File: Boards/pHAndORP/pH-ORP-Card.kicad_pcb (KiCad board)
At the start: 4 copper layers, 80 x 72 mm, 120 parts, among them IC1 PIC32MM0064GPM028, Q1 NX7002AK, Q2 NX7002AK, Q3 NX7002AK, Q4 AO3407A, Q5 MMBT3904, Q6 MMBT3904, Q7 AO3407A, Q8 AO3407A, U1 AP2114H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

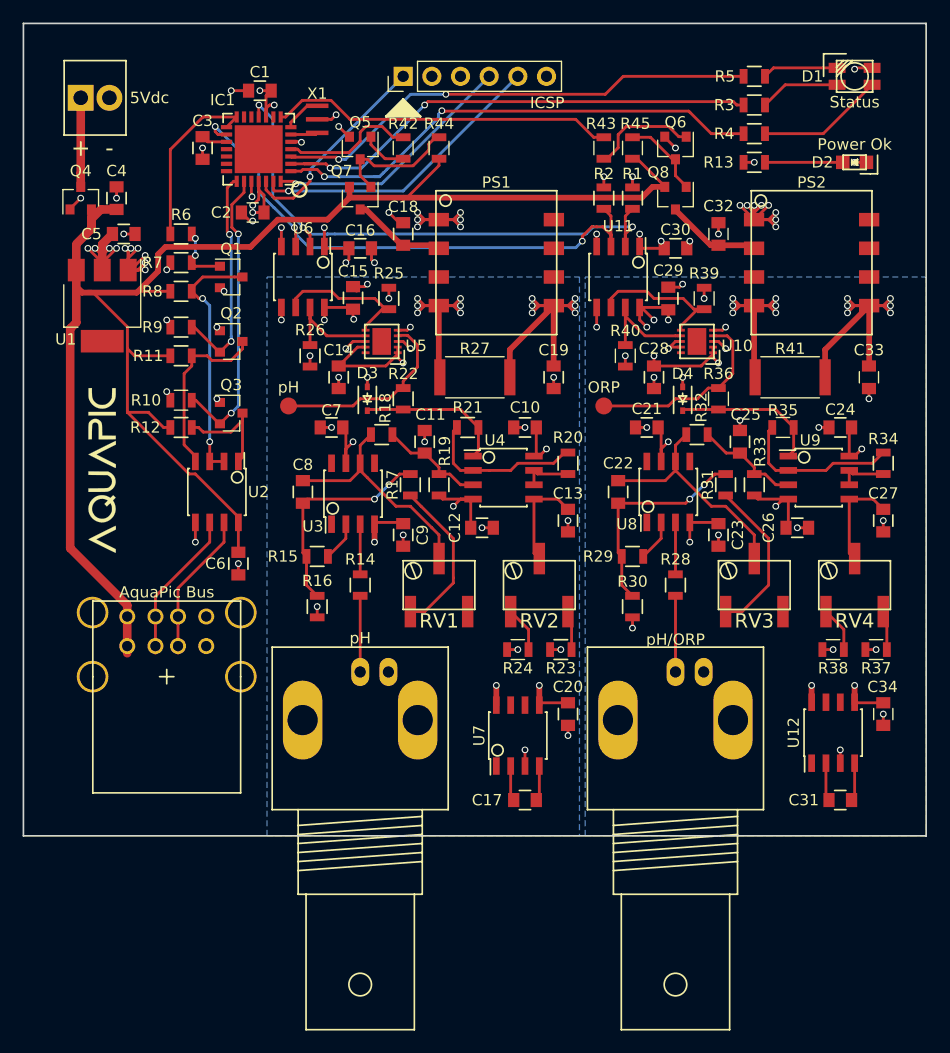
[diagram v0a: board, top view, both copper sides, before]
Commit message: changed power supply switch from p channel to n channel
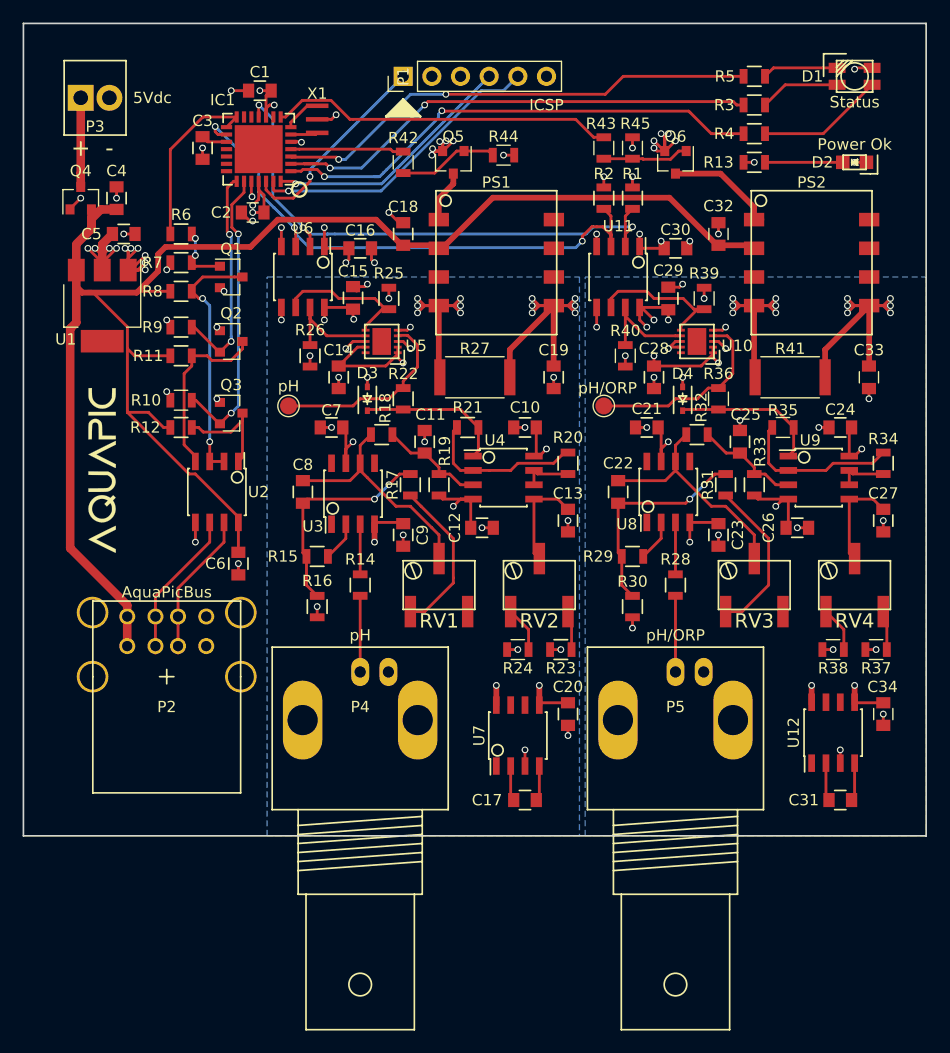
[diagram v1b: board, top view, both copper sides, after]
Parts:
- removed 5Vdc: 2x1 2.54, MyFootPrints:Screw_Header_1x2
- removed AquaPic Bus: usb1.1, MyFootPrints:USB-1.1_Stacked
- removed ICSP: 5x1 2.54, Pin_Headers:Pin_Header_Straight_1x06_Pitch2.54mm
- removed ORP, pH: TEST, Measurement_Points:Measurement_Point_Round-SMD-Pad_Small
- removed Q7, Q8: AO3407A, TO_SOT_Packages_SMD:SOT-23
- removed pH, pH/ORP: BNC, MyFootPrints:BNC_Socket_TYCO-AMP_LargePads
- added P1: ICSP, Connector_PinHeader_2.54mm:PinHeader_1x06_P2.54mm_Vertical, F.Cu at (33.7, -67.3)
- added P2: AquaPicBus, MyFootPrints:USB-1.1_Stacked, F.Cu at (12.7, -14.0)
- added P3: 5Vdc, MyFootPrints:Screw_Header_1x2, F.Cu at (6.35, -65.4)
- added P4: pH, MyFootPrints:BNC_Socket_TYCO-AMP_LargePads, F.Cu at (29.8, -9.53)
- added P5: pH/ORP, MyFootPrints:BNC_Socket_TYCO-AMP_LargePads, F.Cu at (57.8, -9.53)
- added TP1: pH, TestPoint:TestPoint_Pad_D1.5mm, F.Cu at (23.5, -38.1)
- added TP2: pH/ORP, TestPoint:TestPoint_Pad_D1.5mm, F.Cu at (51.4, -38.1)
- Q5, Q6: value MMBT3904 -> NX7002AK
- moved Q5 8.35 mm to (38.1, -59.7)
- moved R44 5.75 mm to (42.5, -60.3), turned to 0 degrees
- moved Q6 1.27 mm to (57.8, -59.7)
- moved R42 1.27 mm to (33.7, -59.7)
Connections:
- C18 pad 1: Net-(C18-Pad1) -> +5V
- C32 pad 1: Net-(C32-Pad1) -> +5V
- PS1 pad 1: GND -> Net-(C18-Pad2)
- PS1 pad 2: Net-(C18-Pad1) -> +5V
- PS2 pad 1: GND -> Net-(C32-Pad2)
- PS2 pad 2: Net-(C32-Pad1) -> +5V
- Q5 pad 3: Net-(Q5-Pad3) -> Net-(C18-Pad2)
- Q6 pad 3: Net-(Q6-Pad3) -> Net-(C32-Pad2)
- R44 pad 1: +5V -> Net-(Q5-Pad1)
- R44 pad 2: Net-(Q5-Pad3) -> GND
- R45 pad 1: +5V -> Net-(Q6-Pad1)
- R45 pad 2: Net-(Q6-Pad3) -> GND
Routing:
- net GND: track 67.3 -> 53.5 mm, vias 42 -> 38
- net Net-(Q5-Pad3): track 11.4 -> 0.00 mm
- net Net-(C32-Pad2): track 0.00 -> 10.6 mm
- net Net-(C32-Pad1): track 8.80 -> 0.00 mm
- net Net-(C18-Pad1): track 8.65 -> 0.00 mm
- net Net-(Q6-Pad3): track 7.46 -> 0.00 mm
- net Net-(C18-Pad2): track 0.00 -> 6.23 mm
- net Net-(Q5-Pad1): track 4.08 -> 8.90 mm
- net +5V: track 164.1 -> 166.4 mm
- net Net-(Q6-Pad1): track 9.54 -> 7.62 mm
- net /En_pH: track 11.9 -> 10.0 mm
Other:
- board text added: "AquaPic pH and ORP Rev 1.1 Goodtime Development Skyler Brandt"
- board text removed: "AquaPic pH and ORP Rev 1 Goodtime Development Skyler Brandt"
